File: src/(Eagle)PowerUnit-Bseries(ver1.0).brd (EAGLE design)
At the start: 100 x 100 mm, 95 parts, among them CON1 XT90PW-M, CON2 XT90PW-F, CON3 XT60PW-F, CON4 XT60PW-F, CON5 XT60PW-F, CON6 XT60PW-F, Q2 SSM3J332R, Q4 SSM3J332R, SW1 SS-12SDP2, U1 LQFP64, U2 MCP2517FD, U3 CH340E, U5 AP63205WU-7, U7 AP331AWG-7, U9 AP331AWG-7, X1 XRCGB40M000F4M00R0

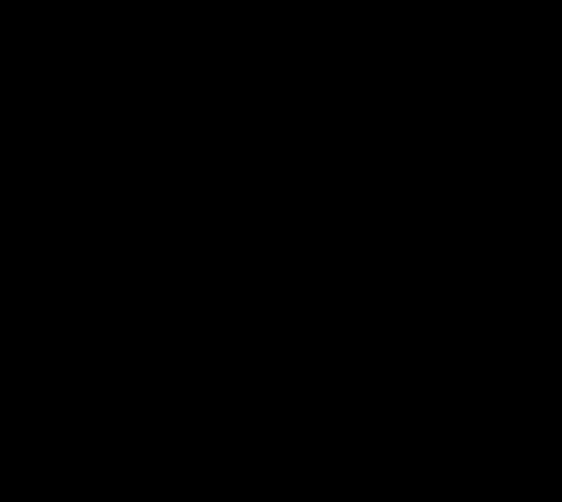
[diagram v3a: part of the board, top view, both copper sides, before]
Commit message: トランシーバ部分の設計終わり(仮)
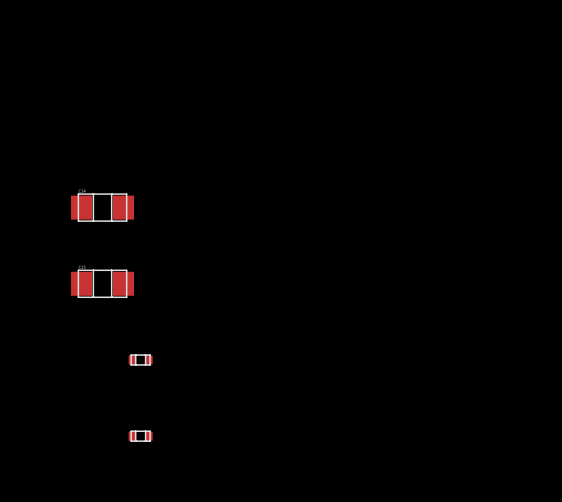
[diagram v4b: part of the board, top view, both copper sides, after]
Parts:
- added C14, C15: GCM188L81H104KA57, GCM188L81H104K57(0.1uF):GCM188L81H104KA57
- added C16, C17: GRM0335C1H120GA01, GRM0335C1H120GA01:GRM0335C1H120GA01
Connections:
- net +3V3: now also C15.P$1
- net +5V: now also C14.P$1
- net GND2: now also C14.P$2, C15.P$2, C16.2, C17.2
- net N$39: now also C17.1
- net N$42: now also C16.1
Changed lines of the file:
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@@
 <attribute name="VALUE" x="43.15" y="35.43" size="0.5" layer="27"/>
+</element>
+<element name="C14" library="GCM188L81H104K57(0.1uF)" package="GCM188L81H104KA57" value="GCM188L81H104KA57" x="-148.59" y="-6.35" smashed="yes">
+<attribute name="NAME" x="-149.39" y="-5.85" size="0.1" layer="21"/>
+</element>
+<element name="C15" library="GCM188L81H104K57(0.1uF)" package="GCM188L81H104KA57" value="GCM188L81H104KA57" x="-148.59" y="-8.89" smashed="yes">
+<attribute name="NAME" x="-149.39" y="-8.39" size="0.1" layer="21"/>
+</element>
+<element name="C16" library="GRM0335C1H120GA01" package="GRM0335C1H120GA01" value="GRM0335C1H120GA01" x="-147.32" y="-11.43" smashed="yes">
+<attribute name="VALUE" x="-148.186" y="-11.1815" size="0.3" layer="27"/>
+</element>
+<element name="C17" library="GRM0335C1H120GA01" package="GRM0335C1H120GA01" value="GRM0335C1H120GA01" x="-147.32" y="-13.97" smashed="yes">
+<attribute name="VALUE" x="-148.186" y="-13.7215" size="0.3" layer="27"/>
 </element>
 </elements>
@@
 <contactref element="U2" pad="VSS"/>
 <contactref element="C13" pad="P$1"/>
+<contactref element="C14" pad="P$2"/>
+<contactref element="C15" pad="P$2"/>
 <contactref element="U$1" pad="VSS"/>
 <contactref element="U$1" pad="EP"/>
-<wire x1="-140.97" y1="99.06" x2="53.91" y2="64.77" width="0" layer="19" extent="1-1"/>
+<contactref element="C17" pad="2"/>
+<contactref element="C16" pad="2"/>
+<wire x1="-147.045" y1="-11.43" x2="-147.045" y2="-13.97" width="0" layer="19" extent="1-1"/>
+<wire x1="-147.89" y1="-8.89" x2="-147.045" y2="-11.43" width="0" layer="19" extent="1-1"/>
+<wire x1="-147.89" y1="-6.35" x2="-147.89" y2="-8.89" width="0" layer="19" extent="1-1"/>
+<wire x1="-140.97" y1="99.06" x2="-147.89" y2="-6.35" width="0" layer="19" extent="1-1"/>
 <wire x1="-33.02" y1="105.41" x2="-140.97" y2="99.06" width="0" layer="19" extent="1-1"/>
 <wire x1="-20.32" y1="60.96" x2="-33.02" y2="105.41" width="0" layer="19" extent="1-1"/>
@@
 <wire x1="62.66" y1="60.96" x2="62.66" y2="57.15" width="0" layer="19" extent="1-1"/>
 <wire x1="64.2" y1="63.5" x2="62.66" y2="60.96" width="0" layer="19" extent="1-1"/>
+<wire x1="53.91" y1="64.77" x2="62.66" y2="60.96" width="0" layer="19" extent="1-1"/>
 <wire x1="11.7" y1="29.21" x2="6.59" y2="41.35" width="0" layer="19" extent="1-1"/>
 <wire x1="11.7" y1="26.67" x2="11.7" y2="29.21" width="0" layer="19" extent="1-1"/>
@@
 <contactref element="C13" pad="P$2"/>
 <contactref element="U$1" pad="VIO"/>
-<wire x1="55.11" y1="51.505" x2="55.31" y2="64.77" width="0" layer="19" extent="1-1"/>
-<wire x1="53.61" y1="51.505" x2="55.11" y2="51.505" width="0" layer="19" extent="1-1"/>
-<wire x1="45.2" y1="43.36" x2="53.61" y2="51.505" width="0" layer="19" extent="1-1"/>
-<wire x1="34.29" y1="43.5" x2="45.2" y2="43.36" width="0" layer="19" extent="1-1"/>
-<wire x1="33.86" y1="48.26" x2="34.29" y2="43.5" width="0" layer="19" extent="1-1"/>
+<contactref element="C15" pad="P$1"/>
+<wire x1="8.89" y1="41.35" x2="-149.29" y2="-8.89" width="0" layer="19" extent="1-1"/>
+<wire x1="8.89" y1="47.55" x2="8.89" y2="41.35" width="0" layer="19" extent="1-1"/>
+<wire x1="24.83" y1="45.72" x2="8.89" y2="47.55" width="0" layer="19" extent="1-1"/>
+<wire x1="33.86" y1="48.26" x2="24.83" y2="45.72" width="0" layer="19" extent="1-1"/>
 <wire x1="33.59" y1="52.07" x2="33.86" y2="48.26" width="0" layer="19" extent="1-1"/>
-<wire x1="24.83" y1="45.72" x2="33.86" y2="48.26" width="0" layer="19" extent="1-1"/>
-<wire x1="8.89" y1="47.55" x2="24.83" y2="45.72" width="0" layer="19" extent="1-1"/>
-<wire x1="8.89" y1="41.35" x2="8.89" y2="47.55" width="0" layer="19" extent="1-1"/>
+<wire x1="34.29" y1="43.5" x2="33.86" y2="48.26" width="0" layer="19" extent="1-1"/>
+<wire x1="45.2" y1="43.36" x2="34.29" y2="43.5" width="0" layer="19" extent="1-1"/>
+<wire x1="53.61" y1="51.505" x2="45.2" y2="43.36" width="0" layer="19" extent="1-1"/>
+<wire x1="55.11" y1="51.505" x2="53.61" y2="51.505" width="0" layer="19" extent="1-1"/>
+<wire x1="55.31" y1="64.77" x2="55.11" y2="51.505" width="0" layer="19" extent="1-1"/>
 </signal>
 <signal name="N$33">
@@
 <contactref element="C10" pad="P$1"/>
 <contactref element="U$1" pad="VDD"/>
-<wire x1="63.82" y1="55.96" x2="65.72" y2="58.64" width="0" layer="19" extent="1-1"/>
-<wire x1="63.77" y1="50.8" x2="63.82" y2="55.96" width="0" layer="19" extent="1-1"/>
-<wire x1="65.77" y1="48.26" x2="63.77" y2="50.8" width="0" layer="19" extent="1-1"/>
-<wire x1="63.82" y1="41.99" x2="65.77" y2="48.26" width="0" layer="19" extent="1-1"/>
+<contactref element="C14" pad="P$1"/>
+<wire x1="11.19" y1="41.35" x2="-149.29" y2="-6.35" width="0" layer="19" extent="1-1"/>
+<wire x1="33.59" y1="54.61" x2="11.19" y2="41.35" width="0" layer="19" extent="1-1"/>
+<wire x1="33.86" y1="57.15" x2="33.59" y2="54.61" width="0" layer="19" extent="1-1"/>
+<wire x1="44.7" y1="40.46" x2="33.59" y2="54.61" width="0" layer="19" extent="1-1"/>
+<wire x1="63.82" y1="41.99" x2="44.7" y2="40.46" width="0" layer="19" extent="1-1"/>
 <wire x1="63.77" y1="36.83" x2="63.82" y2="41.99" width="0" layer="19" extent="1-1"/>
 <wire x1="65.77" y1="34.29" x2="63.77" y2="36.83" width="0" layer="19" extent="1-1"/>
 <wire x1="69.53" y1="40.86" x2="63.82" y2="41.99" width="0" layer="19" extent="1-1"/>
+<wire x1="65.77" y1="48.26" x2="63.82" y2="41.99" width="0" layer="19" extent="1-1"/>
+<wire x1="63.77" y1="50.8" x2="65.77" y2="48.26" width="0" layer="19" extent="1-1"/>
+<wire x1="63.82" y1="55.96" x2="63.77" y2="50.8" width="0" layer="19" extent="1-1"/>
+<wire x1="65.72" y1="58.64" x2="63.82" y2="55.96" width="0" layer="19" extent="1-1"/>
 <wire x1="73.39" y1="48.26" x2="65.77" y2="48.26" width="0" layer="19" extent="1-1"/>
 <wire x1="73.39" y1="34.29" x2="65.77" y2="34.29" width="0" layer="19" extent="1-1"/>
-<wire x1="44.7" y1="40.46" x2="63.82" y2="41.99" width="0" layer="19" extent="1-1"/>
-<wire x1="33.59" y1="54.61" x2="44.7" y2="40.46" width="0" layer="19" extent="1-1"/>
-<wire x1="33.86" y1="57.15" x2="33.59" y2="54.61" width="0" layer="19" extent="1-1"/>
-<wire x1="11.19" y1="41.35" x2="33.59" y2="54.61" width="0" layer="19" extent="1-1"/>
 </signal>
 <signal name="N$35">
@@
 <contactref element="U2" pad="OSC1"/>
 <contactref element="X1" pad="2"/>
-<wire x1="40.64" y1="38.1" x2="45.125" y2="37.33" width="0" layer="19" extent="1-1"/>
+<contactref element="C17" pad="1"/>
+<wire x1="40.64" y1="38.1" x2="-147.595" y2="-13.97" width="0" layer="19" extent="1-1"/>
+<wire x1="45.125" y1="37.33" x2="40.64" y2="38.1" width="0" layer="19" extent="1-1"/>
 </signal>
 <signal name="N$42">
 <contactref element="U2" pad="OSC2"/>
 <contactref element="X1" pad="1"/>
-<wire x1="39.37" y1="38.1" x2="43.775" y2="36.33" width="0" layer="19" extent="1-1"/>
+<contactref element="C16" pad="1"/>
+<wire x1="39.37" y1="38.1" x2="-147.595" y2="-11.43" width="0" layer="19" extent="1-1"/>
+<wire x1="43.775" y1="36.33" x2="39.37" y2="38.1" width="0" layer="19" extent="1-1"/>
 </signal>
 </signals>

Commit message: STM32の電源回り
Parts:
- added C18, C19, C20, C21: GCM188L81H104KA57, GCM188L81H104K57(0.1uF):GCM188L81H104KA57
- added R11: 10k, CR0603:CR0603
- added STLINK: (no value), con-jst-xh:B6B-XH
- moved C14 220.9 mm to (69.8, 26.7)
- moved C15 220.9 mm to (69.8, 24.1)
- moved C16 220.9 mm to (71.1, 21.6)
- moved C17 220.9 mm to (71.1, 19.1)
- moved EDGE4 110.7 mm to (-33.0, 77.5), turned to 0 degrees
- moved CTRL2 15.5 mm to (-55.9, 88.9)
- moved JP1 15.5 mm to (-38.1, 106.7)
- moved LED3 15.5 mm to (-31.8, 108.0)
- moved R2 15.5 mm to (-57.1, 106.7)
- moved R5 15.5 mm to (-2.54, 113.0)
- moved R6 15.5 mm to (-12.7, 113.0)
- moved THRU1 15.5 mm to (-38.1, 88.9)
- moved LED1 15.5 mm to (-6.35, 108.0)
- moved C2 15.5 mm to (-19.1, 113.0)
- moved IRLB-3 15.5 mm to (-34.3, 10.2)
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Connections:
- new net N$45: R11.LEFT, U1.P60
- new net NRST: STLINK.2, U1.P7
- new net SWCLK: STLINK.5, U1.P49
- new net SWDIO: STLINK.3, U1.P46
- new net SWO: STLINK.1, U1.P55
- net +3V3: now also C18.P$1, C19.P$1, C20.P$1, C21.P$1, STLINK.6, U1.P19, U1.P32, U1.P48, U1.P64
- net DIR1: now also U1.P24
- net DIR2: now also U1.P25
- net DIR3: now also U1.P26
- net DIR4: now also U1.P27
- net GND: now also C3.P$1, EDGE1.P$24, EDGE2.P$24, EDGE3.P$24, EDGE4.P$24, LED2.K, STLINK.4
- net GND2: now also C18.P$2, C19.P$2, C20.P$2, C21.P$2, R11.RIGHT, U1.P18, U1.P31, U1.P47, U1.P63; no longer C3.P$1, EDGE1.P$24, EDGE2.P$24, EDGE3.P$24, EDGE4.P$24, LED2.K
- net PWM1: now also U1.P50
- net PWM2: now also U1.P15
- net PWM3: now also U1.P29
- net PWM4: now also U1.P28

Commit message: OSC周り
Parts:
- added B1: CS11029.5F100, CS11029.5F100:CS11029.5F100
- added BOOTMODE: (no value), pinhead:1X02
- added C22, C25, C26: GCM188L81H104KA57, GCM188L81H104K57(0.1uF):GCM188L81H104KA57
- added C23: GRM21BC72A105KE01, GRM21BC72A105KE01(1uF):GRM21BC72A105KE01
- added C24: GRM31CR71H475KA12, GRM31CR71H475KA12:GRM31CR71H475KA12
- added FB1: BLM18KG121TN1D, BLM18KG121TN1D:BLM18KG121TN1D
- added R12, R13: 2.4Meg, CR0603:CR0603
- added R14, R16, R17, R25, R26: 0, CR0603:CR0603
- added R15: 100k, CR0603:CR0603
- added X2: RH100-24.000-18-1020-EXT-TR, RH100-24.000-18-1020-EXT-TR:RH100-24.000-18-1020-EXT-TR
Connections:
- net N$38 renamed VM2
- net N$44 renamed VM1
- new net BOOT0: BOOTMODE.1, R11.LEFT, U1.P60
- new net DIP_SW3: R25.RIGHT, U1.P52
- new net DIP_SW4: R26.RIGHT, U1.P51
- new net N$38: R14.LEFT, U2.OSC2
- new net N$44: R16.LEFT, U1.P16
- new net N$46: C22.P$1, C23.P$1, FB1.2, U1.P13
- new net N$48: C24.1, U1.P30
- new net N$49: U1.P5, X2.1
- new net N$50: U1.P6, X2.3
- net +3V3: now also BOOTMODE.2, C25.P$1, FB1.1, U1.P1
- net GND2: now also B1.3, C22.P$2, C23.P$2, C24.2, C25.P$2, C26.P$1, C26.P$2, R15.LEFT, U1.P12, X2.2, X2.4
- net N$42: now also R14.RIGHT; no longer U2.OSC2
- net N$43: now also R12.LEFT
- net N$45: now also R17.LEFT, U1.P17; no longer R11.LEFT, U1.P60
- net N$47: now also R12.RIGHT
- net N$51: now also R13.LEFT
- net N$53: now also R13.RIGHT
- net NRST: now also B1.1
- net PWM4: now also R15.RIGHT
- net USART_RX: now also R17.RIGHT, R26.LEFT; no longer U1.P17
- net USART_TX: now also R16.RIGHT, R25.LEFT; no longer U1.P16

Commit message: DIPスイッチ周り
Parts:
- added C27, C28: GRM0335C1E240GA01D, GRM0335C1E240GA01D:GRM0335C1E240GA01D
- added C29, C30: GRM0335C1H150FA01D, GRM0335C1H150FA01D:GRM0335C1H120GA01
- added C31, C32, C33, C34: GCM188L81H104KA57, GCM188L81H104K57(0.1uF):GCM188L81H104KA57
- added JP2, JP3, JP4, JP5: (no value), con-jst-xh:B5B-XH
- added R27, R28: 0, CR0603:CR0603
- added R29, R30, R31, R41: 10k, CR0603:CR0603
- added SW2: RDS-16S-1055-SMT-TR, RDS-16S-1055-SMT-TR:RDS-16S-1055-SMT-TR
- added X3: 32.768K12.5PI/MC306, 32.768K12.5PI:32.768K12.5PI/MC306
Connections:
- new net DIP_SW1: R41.RIGHT, SW2.1
- new net DIP_SW2: R31.RIGHT, SW2.2
- new net ENC1_A: JP2.3, U1.P41
- new net ENC1_B: JP2.5, U1.P42
- new net ENC2_A: JP4.3, U1.P22
- new net ENC2_B: JP4.5, U1.P23
- new net ENC3_A: JP3.3, U1.P58
- new net ENC3_B: JP3.5, U1.P59
- new net ENC4_A: JP5.3, U1.P37
- new net ENC4_B: JP5.5, U1.P38
- new net N$52: R27.RIGHT, U1.P6
- new net N$54: C28.2, R27.LEFT, X2.3
- new net N$56: C30.2, R28.LEFT, X3.1
- new net N$57: C29.2, U1.P3, X3.4
- net +3V3: now also SW2.C1, SW2.C2
- net +5V: now also C31.P$1, C32.P$1, C33.P$1, C34.P$1, JP2.4, JP3.4, JP4.4, JP5.4
- net DIP_SW3: now also R30.RIGHT, SW2.4
- net DIP_SW4: now also R29.RIGHT, SW2.8
- net GND2: now also C27.1, C28.1, C29.1, C30.1, C31.P$2, C32.P$2, C33.P$2, C34.P$2, JP2.1, JP3.1, JP4.1, JP5.1, R29.LEFT, R30.LEFT, R31.LEFT, R41.LEFT
- net N$49: now also C27.2
- net N$50: now also R28.RIGHT, U1.P4; no longer U1.P6, X2.3

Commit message: RJ45の追加
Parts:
- removed STLINK: (no value), con-jst-xh:B6B-XH
- added B2: PTS645SM95SMTR92LFS, PTS645SM95SMTR92LFS:PTS645SM95SMTR92LFS
- added C35, C36: GCM188L81H104KA57, GCM188L81H104K57(0.1uF):GCM188L81H104KA57
- added LED5, LED6, LED7: SML-E12V8WT86, SML-E12V8WT86:SML-E12V8WT86
- added ML1: 3220-14-0100-00, 3220-14-0100-00:3220-14-0100-00
- added R42, R43, R44: 100, CR0603:CR0603
- added R45, R46, R47, R48, R49, R50: 10k, CR0603:CR0603
- added R51, R52, R53: 0, CR0603:CR0603
- added SW3: SSSS213202, SSSS213202:SSSS213202
- moved SW2 207.5 mm to (99.1, 87.6), turned to 90 degrees
- moved C1 189.7 mm to (119.4, 36.8), turned to 90 degrees
- moved TLP1 185.0 mm to (99.1, 14.0), turned to 90 degrees
- moved P-8 177.9 mm to (101.6, 22.9), turned to 90 degrees
- moved IRLB-4 176.2 mm to (120.7, 55.9), turned to 90 degrees
- moved P-7 170.2 mm to (101.6, 30.5), turned to 90 degrees
- moved IRLB-3 166.5 mm to (120.7, 71.1), turned to 90 degrees
- moved P-6 162.8 mm to (101.6, 38.1), turned to 90 degrees
- moved IRLB-2 159.1 mm to (120.7, 86.4), turned to 90 degrees
- moved P-5 155.8 mm to (101.6, 45.7), turned to 90 degrees
- moved CON1 155.7 mm to (156.2, 96.5), turned to 90 degrees
- moved IRLB-1 154.4 mm to (120.7, 101.6), turned to 90 degrees
- moved P-4 149.3 mm to (101.6, 53.3), turned to 90 degrees
- moved CON3 144.2 mm to (156.2, 53.3), turned to 90 degrees
- moved R41 143.9 mm to (8.89, 78.7), turned to 90 degrees
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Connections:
- new net ALIVE_LED: R42.RIGHT, U1.P45
- new net COM_LED: R43.RIGHT, U1.P44
- new net DEBUG_BT: C35.P$1, R46.RIGHT, R47.LEFT, R47.RIGHT, U1.P56
- new net DEBUG_LED: R44.RIGHT, U1.P43
- new net DEBUG_SW: R50.RIGHT, U1.P57
- new net N$58: LED5.A, R42.LEFT
- new net N$59: LED6.A, R43.LEFT
- new net N$60: LED7.A, R44.LEFT
- new net N$61: B2.4, R45.LEFT
- new net N$62: B2.3, R46.LEFT
- new net N$63: R48.LEFT, R49.RIGHT, SW3.3A, SW3.3B
- new net N$64: ML1.13, R51.LEFT
- new net N$65: C36.P$1, R48.RIGHT, R50.LEFT
- new net N$66: ML1.14, R52.RIGHT
- new net N$67: ML1.10, R53.RIGHT
- net +3V3: now also B2.1, ML1.3, SW3.2A, SW3.2B; no longer STLINK.6
- net DIP_SW1: now also U1.P54
- net DIP_SW2: now also U1.P53
- net GND: no longer STLINK.4
- net GND2: now also C35.P$2, C36.P$2, LED5.K, LED6.K, LED7.K, ML1.11, ML1.5, ML1.7, R45.RIGHT, R49.LEFT; no longer C26.P$1
- net NRST: now also C26.P$1, ML1.12; no longer STLINK.2
- net PWM1: now also R53.LEFT
- net SWCLK: now also ML1.6; no longer STLINK.5
- net SWDIO: now also ML1.4; no longer STLINK.3
- net SWO: now also ML1.8; no longer STLINK.1
- net USART_RX: now also R51.RIGHT
- net USART_TX: now also R52.LEFT
